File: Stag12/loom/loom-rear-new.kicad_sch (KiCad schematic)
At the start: 28 parts, among them J12 XT60H-M, J19 ASHD114-1SN-S25, J3 RING TERMINAL ON MAIN ROLL HO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

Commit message: Renamed EXC to PWR in rear loom
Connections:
- net ACCU.EXC renamed ACCU.PWR
- net BRAKE.LIGHT.EXC renamed BRAKE.LIGHT.PWR
- net BSPD.CUR_SEN.EXC renamed BSPD.CUR_SEN.PWR
- net CAN.AB.EXC renamed AIRBRIDGE.PWR
- net CAN.B.EXC renamed CAN.B.PWR
- net CAN.F.EXC renamed CAN.F.PWR
- net DASH.EXC renamed DASH.PWR
- net FAN.EXC renamed FAN.PWR
- net HVSENSE.EXC renamed HVSENSE.PWR
- net INV.EXC renamed INV.PWR
- net L120.EXC renamed L120.PWR
- net L120.SENSOR.5V.EXC renamed L120.SENSOR.5V.PWR
- net LV_BOX.EXC renamed LV_BOX.PWR
- net MOTOR.TEMP.EXC renamed MOTOR.TEMP.PWR
- net PEDALBOX.EXC renamed PEDALBOX.PWR
- net PUMP1.EXC renamed PUMP1.PWR
- net PUMP2.EXC renamed PUMP2.PWR
- net RESOLVER.EXC renamed RESOLVER.PWR
- net SPARE.EXC renamed SPARE.PWR
- net TSAC.HVS.EXC renamed TSAC.HVS.PWR
- net TSAL.DASH.EXC renamed TSAL.DASH.PWR
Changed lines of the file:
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@@
 	)
 	(bus_alias "BSPD.CUR_SEN"
-		(members "CT.SIG" "BSPD.CUR_SEN.EXC" "BSPD.CUR_SEN.GND")
+		(members "CT.SIG" "BSPD.CUR_SEN.PWR" "BSPD.CUR_SEN.GND")
 	)
 	(bus_alias "BSPD.SIM"
@@
 	)
 	(bus_alias "DASH.REAR.SIG"
-		(members "TS.DETECTED.DASH" "DASH.TS.OFF" "TSAL.DASH.EXC")
+		(members "TS.DETECTED.DASH" "DASH.TS.OFF" "TSAL.DASH.PWR")
 	)
 	(bus_alias "INV.RS232"
@@
 	)
 	(bus_alias "ONLYFANS"
-		(members "FAN.EXC" "FAN.L.PWM" "FAN.L.TACH" "FAN.R.PWM" "FAN.R.TACH" "FAN.GND")
+		(members "FAN.PWR" "FAN.L.PWM" "FAN.L.TACH" "FAN.R.PWM" "FAN.R.TACH" "FAN.GND")
 	)
 	(bus_alias "REAR_BOX"
-		(members "FAN.EXC" "FAN.GND" "FAN.L.PWM" "FAN.R.PWM" "FAN.L.TACH" "FAN.R.TACH"
-			"BRAKE.LIGHT.EXC" "BRAKE.LIGHT.GND" "CAN.B.HIGH" "CAN.B.LOW" "CAN.B.EXC"
+		(members "FAN.PWR" "FAN.GND" "FAN.L.PWM" "FAN.R.PWM" "FAN.L.TACH" "FAN.R.TACH"
+			"BRAKE.LIGHT.PWR" "BRAKE.LIGHT.GND" "CAN.B.HIGH" "CAN.B.LOW" "CAN.B.PWR"
 			"CAN.B.GND" "WHLSPD.RL.PWR" "WHLSPD.RL.SIG" "WHLSPD.RL.GND" "WHLSPD.RR.PWR"
 			"WHLSPD.RR.SIG" "WHLSPD.RR.GND" "WHLACL.RL.PWR" "WHLACL.RL.SIG" "WHLACL.RL.GND"
@@
 	)
 	(bus_alias "RESOLVER"
-		(members "RESOLVER.EXC" "RESOLVER.GND" "RESOLVER.SIN+" "RESOLVER.SIN-"
+		(members "RESOLVER.PWR" "RESOLVER.GND" "RESOLVER.SIN+" "RESOLVER.SIN-"
 			"RESOLVER.COS+" "RESOLVER.COS-"
 		)
@@
 		)
 	)
-	(label "L120.EXC"
+	(label "L120.PWR"
 		(at 417.83 48.26 180)
 		(effects
@@
 		)
 	)
-	(label "DASH.EXC"
+	(label "DASH.PWR"
 		(at 53.975 33.02 0)
 		(effects
@@
 		)
 	)
-	(label "HVSENSE.EXC"
+	(label "HVSENSE.PWR"
 		(at 714.375 349.885 0)
 		(effects
@@
 		)
 	)
-	(label "CAN.AB.PWR"
+	(label "AIRBRIDGE.PWR"
 		(at 473.71 316.23 0)
 		(effects
@@
 		)
 	)
-	(label "CAN.AB.EXC"
+	(label "AIRBRIDGE.PWR"
 		(at 486.41 28.575 180)
 		(effects
@@
 		)
 	)
-	(label "LV_BOX.EXC"
+	(label "LV_BOX.PWR"
 		(at 486.41 23.495 180)
 		(effects
@@
 		)
 	)
-	(label "PUMP1.EXC"
+	(label "PUMP1.PWR"
 		(at 486.41 99.06 180)
 		(effects
@@
 		)
 	)
-	(label "CAN.B.EXC"
+	(label "CAN.B.PWR"
 		(at 417.83 40.64 180)
 		(effects
@@
 		)
 	)
-	(label "LV_BOX.EXC"
+	(label "LV_BOX.PWR"
 		(at 417.83 33.02 180)
 		(effects
@@
 		)
 	)
-	(label "PUMP2.EXC"
+	(label "PUMP2.PWR"
 		(at 208.28 544.83 90)
 		(effects
@@
 		)
 	)
-	(label "DASH.EXC"
+	(label "DASH.PWR"
 		(at 486.41 59.055 180)
 		(effects
@@
 		)
 	)
-	(label "CAN.AB.GND"
+	(label "AIRBRIDGE.GND"
 		(at 305.435 544.195 90)
 		(effects
@@
 		)
 	)
-	(label "BSPD.CUR_SEN.EXC"
+	(label "BSPD.CUR_SEN.PWR"
 		(at 53.975 43.18 0)
 		(effects
@@
 		)
 	)
-	(label "CAN.B.EXC"
+	(label "CAN.B.PWR"
 		(at 52.07 518.16 0)
 		(effects
@@
 		)
 	)
-	(label "CAN.B.EXC"
+	(label "CAN.B.PWR"
 		(at 52.07 449.58 0)
 		(effects
@@
 		)
 	)
-	(label "TSAL.EXC"
+	(label "TSAL.PWR"
 		(at 486.41 91.44 180)
 		(effects
@@
 		)
 	)
-	(label "INV.EXC"
+	(label "INV.PWR"
 		(at 52.07 312.42 0)
 		(effects
@@
 		)
 	)
-	(label "L120.EXC"
+	(label "L120.PWR"
 		(at 486.41 56.515 180)
 		(effects
@@
 		)
 	)
-	(label "PUMP1.EXC"
+	(label "PUMP1.PWR"
 		(at 198.12 544.83 90)
 		(effects
@@
 		)
 	)
-	(label "ACCU.EXC"
+	(label "ACCU.PWR"
 		(at 486.41 53.975 180)
 		(effects
@@
 		)
 	)
-	(label "PEDALBOX.EXC"
+	(label "PEDALBOX.PWR"
 		(at 486.41 26.035 180)
 		(effects
@@
 		)
 	)
-	(label "BSPD.CUR_SEN.EXC"
+	(label "BSPD.CUR_SEN.PWR"
 		(at 714.375 354.965 0)
 		(effects
@@
 		)
 	)
-	(label "CAN.AB.EXC"
+	(label "AIRBRIDGE.PWR"
 		(at 417.83 38.1 180)
 		(effects
@@
 		)
 	)
-	(label "TSAC.HVS.EXC"
+	(label "TSAC.HVS.PWR"
 		(at 714.375 277.495 0)
 		(effects
@@
 		)
 	)
-	(label "FAN.EXC"
+	(label "FAN.PWR"
 		(at 486.41 93.98 180)
 		(effects
@@
 		)
 	)
-	(label "DASH.EXC"
+	(label "DASH.PWR"
 		(at 417.83 50.8 180)
 		(effects
@@
 		)
 	)
-	(label "INV.EXC"
+	(label "INV.PWR"
 		(at 486.41 104.14 180)
 		(effects
@@
 		)
 	)
-	(label "L120.SENSOR.5V.EXC"
+	(label "L120.SENSOR.5V.PWR"
 		(at 719.455 497.205 0)
 		(effects
@@
 		)
 	)
-	(label "PUMP2.EXC"
+	(label "PUMP2.PWR"
 		(at 486.41 101.6 180)
 		(effects
@@
 		)
 	)
-	(label "PEDALBOX.EXC"
+	(label "PEDALBOX.PWR"
 		(at 417.83 35.56 180)
 		(effects
@@
 		)
 	)
-	(label "BRAKE.LIGHT.EXC"
+	(label "BRAKE.LIGHT.PWR"
 		(at 486.41 96.52 180)
 		(effects
@@
 		)
 	)
-	(label "MOTOR.TEMP.EXC"
+	(label "MOTOR.TEMP.PWR"
 		(at 52.07 193.04 0)
 		(effects
@@
 		)
 	)
-	(label "L120.EXC"
+	(label "L120.PWR"
 		(at 714.375 487.045 0)
 		(effects
@@
 		)
 	)
-	(label "ACCU.EXC"
+	(label "ACCU.PWR"
 		(at 417.83 45.72 180)
 		(effects
@@
 		)
 	)
-	(label "RESOLVER.EXC"
+	(label "RESOLVER.PWR"
 		(at 52.07 336.55 0)
 		(effects
@@
 		)
 	)
-	(label "BRAKE.LIGHT.EXC"
+	(label "BRAKE.LIGHT.PWR"
 		(at 52.07 502.92 0)
 		(effects
@@
 		)
 	)
-	(label "TSAL.DASH.EXC"
+	(label "TSAL.DASH.PWR"
 		(at 714.375 219.075 0)
 		(effects
@@
 		)
 	)
-	(label "FAN.EXC"
+	(label "FAN.PWR"
 		(at 52.07 487.68 0)
 		(effects
@@
 		)
 	)
-	(label "CAN.F.EXC"
+	(label "CAN.F.PWR"
 		(at 486.41 51.435 180)
 		(effects
@@
 		)
 	)
-	(label "RESOLVER.EXC"
+	(label "RESOLVER.PWR"
 		(at 52.07 297.18 0)
 		(effects
@@
 		)
 	)
-	(label "L120.SENSOR.5V.EXC"
+	(label "L120.SENSOR.5V.PWR"
 		(at 714.375 423.545 0)
 		(effects
@@
 		)
 	)
-	(label "TSAL.DASH.EXC"
+	(label "TSAL.DASH.PWR"
 		(at 53.975 66.04 0)
 		(effects
@@
 		)
 	)
-	(label "CAN.F.EXC"
+	(label "CAN.F.PWR"
 		(at 417.83 43.18 180)
 		(effects
@@
 		)
 	)
-	(label "CAN.B.EXC"
+	(label "CAN.B.PWR"
 		(at 486.41 48.895 180)
 		(effects
@@
 		)
 	)
-	(label "CAN.AB.GND"
+	(label "AIRBRIDGE.GND"
 		(at 473.71 318.77 0)
 		(effects
@@
 		)
 	)
-	(label "CAN.B.EXC"
+	(label "CAN.B.PWR"
 		(at 52.07 469.265 0)
 		(effects
@@
 		)
 	)
-	(label "TSAL.EXC"
+	(label "TSAL.PWR"
 		(at 715.01 55.88 0)
 		(effects
@@
 		)
 	)
-	(label "HVSENSE.EXC"
+	(label "HVSENSE.PWR"
 		(at 714.375 259.715 0)
 		(effects
@@
 		)
 	)
-	(label "PEDALBOX.EXC"
+	(label "PEDALBOX.PWR"
 		(at 53.975 55.88 0)
 		(effects
@@
 		)
 	)
-	(label "SPARE.EXC"
+	(label "SPARE.PWR"
 		(at 719.455 522.605 0)
 		(effects
@@
 		)
 	)
-	(label "LV_BOX.EXC"
+	(label "LV_BOX.PWR"
 		(at 714.375 213.995 0)
 		(effects
@@
 		)
 	)
-	(label "ACCU.EXC"
+	(label "ACCU.PWR"
 		(at 715.01 60.96 0)
 		(effects

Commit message: Reserved Autosport for pedalbox
Pedal box loom near completion, pending connector spec

VCU is now connector hell
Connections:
- net PEDALBOX.PWR: no longer Conn20.13
- net BSPD.PWR: now reaches Conn30.9
- net BSPD.PWR: now also Conn20.13
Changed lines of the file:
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@@
 	)
 	(bus_entry
-		(at 462.915 157.48)
+		(at 454.025 157.48)
 		(size 2.54 -2.54)
 		(stroke
@@
 	)
 	(bus_entry
-		(at 462.915 152.4)
+		(at 454.025 152.4)
 		(size 2.54 -2.54)
 		(stroke
@@
 	)
 	(bus_entry
-		(at 462.915 160.02)
+		(at 454.025 160.02)
 		(size 2.54 -2.54)
 		(stroke
@@
 	)
 	(bus_entry
-		(at 462.915 154.94)
+		(at 454.025 154.94)
 		(size 2.54 -2.54)
 		(stroke
@@
 		)
 	)
+	(wire
+		(pts
+			(xy 495.3 160.02) (xy 460.375 160.02)
+		)
+		(stroke
+			(width 0)
+			(type default)
+		)
+	)
 	(polyline
 		(pts
@@
 	(wire
 		(pts
-			(xy 465.455 149.86) (xy 495.3 149.86)
+			(xy 456.565 149.86) (xy 495.3 149.86)
 		)
 		(stroke
@@
 		)
 	)
-	(wire
-		(pts
-			(xy 417.83 35.56) (xy 365.125 35.56)
-		)
-		(stroke
-			(width 0)
-			(type default)
-		)
-	)
 	(polyline
 		(pts
@@
 	(wire
 		(pts
+			(xy 460.375 160.02) (xy 460.375 162.56)
+		)
+		(stroke
+			(width 0)
+			(type default)
+		)
+	)
+	(wire
+		(pts
 			(xy 441.325 295.91) (xy 441.325 236.855)
 		)
@@
 	(bus
 		(pts
-			(xy 462.915 186.055) (xy 467.995 191.135)
+			(xy 454.025 186.055) (xy 459.105 191.135)
 		)
 		(stroke
@@
 	(bus
 		(pts
-			(xy 467.995 191.135) (xy 648.97 191.135)
+			(xy 459.105 191.135) (xy 648.97 191.135)
 		)
 		(stroke
@@
 	(bus
 		(pts
-			(xy 462.915 154.94) (xy 462.915 157.48)
+			(xy 454.025 154.94) (xy 454.025 157.48)
 		)
 		(stroke
@@
 		)
 	)
+	(wire
+		(pts
+			(xy 382.905 162.56) (xy 460.375 162.56)
+		)
+		(stroke
+			(width 0)
+			(type default)
+		)
+	)
 	(bus
 		(pts
@@
 	(wire
 		(pts
-			(xy 465.455 157.48) (xy 495.3 157.48)
+			(xy 456.565 157.48) (xy 495.3 157.48)
 		)
 		(stroke
@@
 	(wire
 		(pts
-			(xy 465.455 154.94) (xy 495.3 154.94)
+			(xy 456.565 154.94) (xy 495.3 154.94)
 		)
 		(stroke
@@
 	(wire
 		(pts
-			(xy 365.125 35.56) (xy 365.125 55.88)
-		)
-		(stroke
-			(width 0)
-			(type default)
-		)
-	)
-	(wire
-		(pts
 			(xy 748.03 226.695) (xy 694.69 226.695)
 		)
@@
 	(bus
 		(pts
-			(xy 462.915 160.02) (xy 462.915 186.055)
+			(xy 454.025 160.02) (xy 454.025 186.055)
 		)
 		(stroke
@@
 	(wire
 		(pts
-			(xy 465.455 152.4) (xy 495.3 152.4)
+			(xy 456.565 152.4) (xy 495.3 152.4)
 		)
 		(stroke
@@
 	(bus
 		(pts
-			(xy 462.915 157.48) (xy 462.915 160.02)
+			(xy 454.025 157.48) (xy 454.025 160.02)
 		)
 		(stroke
@@
 	(wire
 		(pts
-			(xy 52.07 55.88) (xy 365.125 55.88)
+			(xy 52.07 55.88) (xy 382.905 55.88)
 		)
 		(stroke
@@
 	(bus
 		(pts
-			(xy 462.915 152.4) (xy 462.915 154.94)
+			(xy 454.025 152.4) (xy 454.025 154.94)
 		)
 		(stroke
@@
 	(wire
 		(pts
+			(xy 381 35.56) (xy 417.83 35.56)
+		)
+		(stroke
+			(width 0)
+			(type default)
+		)
+	)
+	(wire
+		(pts
 			(xy 74.93 409.575) (xy 74.93 422.275)
 		)
@@
 	(wire
 		(pts
+			(xy 382.905 55.88) (xy 382.905 162.56)
+		)
+		(stroke
+			(width 0)
+			(type default)
+		)
+	)
+	(wire
+		(pts
 			(xy 210.82 513.08) (xy 210.82 544.83)
 		)
@@
 		)
 	)
-	(label "PEDALBOX.PWR"
+	(label "BSPD.PWR"
 		(at 53.975 55.88 0)
 		(effects
@@
 		(effects
 			(font
+				(size 1.27 1.27)
+			)
+			(justify left bottom)
+		)
+	)
+	(label "BSPD.PWR"
+		(at 476.885 160.02 0)
+		(effects
+			(font

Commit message: More progress on front loom
autosport my beloved
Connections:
- net BSPD.CUR_SEN.SIG is gone; now on net CT.SIG: Conn74.6
- net CAN.F.PWR: now also Conn20.26
- net CAN.C.L: now reaches Conn20.46
- net CAN.C.L: now also Conn17.18, Conn22.11, Conn31.9, Conn50.20, Conn50.36, Conn51.1, Conn53.1
- net CAN.C.H: now reaches Conn20.47
- net CAN.C.H: now also Conn17.19, Conn22.33, Conn31.10, Conn50.19, Conn50.35, Conn51.2, Conn53.2
- net BSPD.CUR_SEN.GND: no longer names the net of Conn20.9
- net BSPD.CUR_SEN.GND: no longer Conn74.5
- net BSPD.CUR_SEN.PWR renamed BSPD.CT.PWR
- net BSPD.CT.PWR: now also Conn20.2; no longer Conn20.8
- removed net CAN.C.HIGH: Conn17.19, Conn20.3, Conn22.33, Conn31.10, Conn50.19, Conn50.35, Conn51.2, Conn53.2
- removed net CAN.C.LOW: Conn17.18, Conn20.2, Conn22.11, Conn31.9, Conn50.20, Conn50.36, Conn51.1, Conn53.1
- new net BSPD.CT.GND: Conn20.3, Conn74.5
- new net BSPD.CT.SHLD: Conn20.8
- no-connect marks 46 -> 44

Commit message: Rear loom nearly complete
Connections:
- net CAN.F.PWR: now also Conn20.43; no longer Conn20.26
- net L120.AV1: now reaches Conn20.27
- net L120.AV2: now reaches Conn20.28
- net L120.AV3: now reaches Conn20.29
- net L120.AV4: now reaches Conn20.30
- net L120.AV5: now reaches Conn20.31
- net L120.AV6: now reaches Conn20.32
- net CAN.F.GND: now reaches Conn20.42
- net CAN.F.H: now reaches Conn20.44
- net CAN.F.H: now also Conn50.27
- net CAN.F.L: now reaches Conn20.45
- net CAN.F.L: now also Conn50.28
- net CAN.F.HIGH renamed L120.5V.AUX
- net L120.5V.AUX: no longer Conn50.27
- net CAN.F.LOW renamed L120.8V.AUX
- net L120.8V.AUX: no longer Conn50.28
- net PEDALBOX.PWR: no longer names the net of Conn31.2, Conn51.4
- net PEDALBOX.PWR: no longer Conn53.4
- new net L120.AGND.SHLD: Conn20.26
- no-connect marks 44 -> 43
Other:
- moved on the sheet: Conn30, Conn31, Conn32, J19

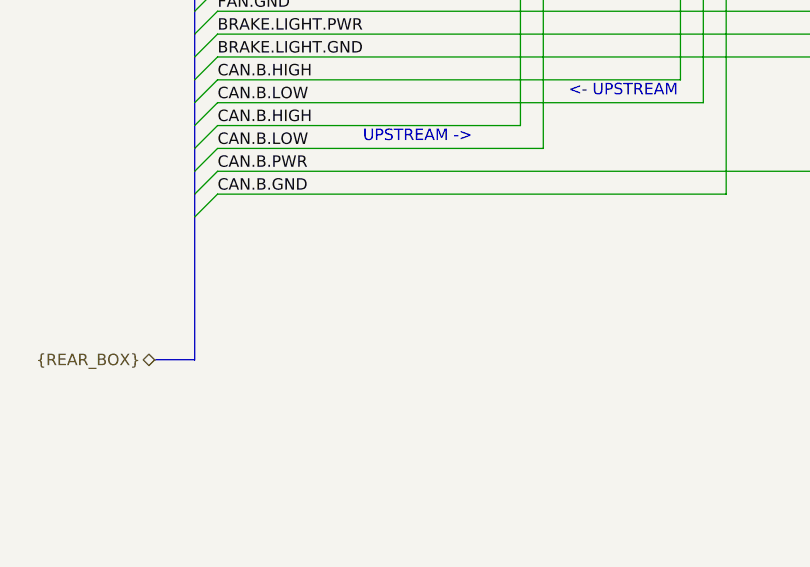
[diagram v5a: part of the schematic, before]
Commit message: More loom notes
autosport crimp selection hell
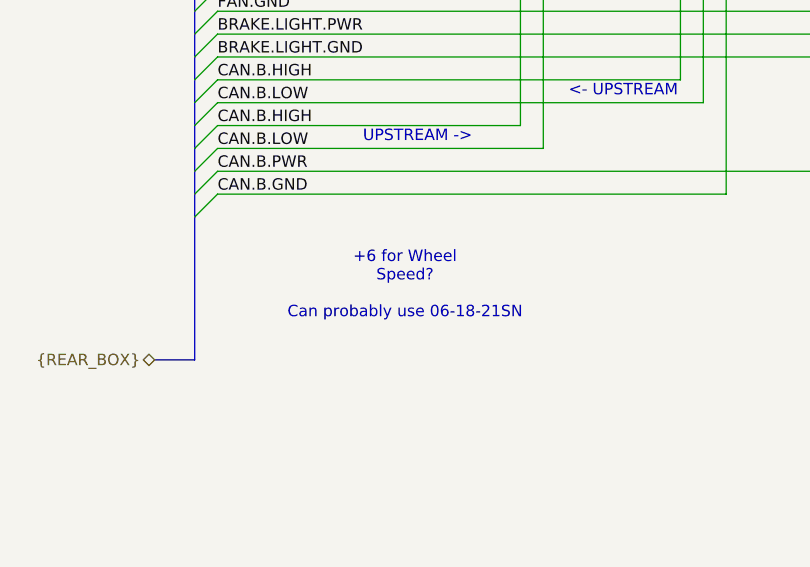
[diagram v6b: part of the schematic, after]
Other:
- note added: "+6 for Wheel Speed? Can probably use 06-18-21SN"
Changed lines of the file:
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@@
+		)
+	)
+	(text "+6 for Wheel\nSpeed?\n\nCan probably use 06-18-21SN"
+		(exclude_from_sim no)
+		(at 72.898 530.86 0)
+		(effects
+			(font
+				(size 1.27 1.27)
+			)
 		)
 	)

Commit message: idfk
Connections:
- net L120.AGND.SHLD is gone; now on net CAN.F.PWR: Conn20.26
- net CAN.F.PWR: no longer Conn20.43
- net PEDALBOX.PWR: now reaches Conn31.2, Conn51.4
- net PEDALBOX.PWR: now also Conn53.4
- net CAN.F.GND: no longer names the net of Conn20.42
- net CAN.F.H: no longer names the net of Conn20.44
- net CAN.F.H: no longer Conn50.27
- net CAN.F.L: no longer names the net of Conn20.45
- net CAN.F.L: no longer Conn50.28
- net L120.5V.AUX renamed CAN.F.HIGH
- net CAN.F.HIGH: now also Conn50.27
- net L120.8V.AUX renamed CAN.F.LOW
- net CAN.F.LOW: now also Conn50.28
- net L120.AV1: no longer names the net of Conn20.27
- net L120.AV2: no longer names the net of Conn20.28
- net L120.AV3: no longer names the net of Conn20.29
- net L120.AV4: no longer names the net of Conn20.30
- net L120.AV5: no longer names the net of Conn20.31
- net L120.AV6: no longer names the net of Conn20.32
- no-connect marks 43 -> 44
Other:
- note added: "/\ ???"
- note added: "???"
- note removed: "+6 for Wheel Speed? Can probably use 06-18-21SN"
- moved on the sheet: Conn30, Conn31, Conn32, J19

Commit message: Updated connector locations
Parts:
- removed Conn72: TODO: CHECK CONNECTOR, symbol Connectors_SUFST:Current Sensor Connector
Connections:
- net INV.PWR: now also Conn23.8
- net RESOLVER.PWR: no longer Conn23.17
- net IN.4: now reaches Conn31.16
- net IN.5: now reaches Conn31.17
- net IN.6: now reaches Conn31.18
- net IN.7: now reaches Conn31.19
- net IN.8: now reaches Conn31.20
- net IN.9: now reaches Conn31.21
- net IN.10: now reaches Conn31.22
- net IN.11: now reaches Conn31.23
- net IN.12: now reaches Conn31.24
- net IN.1: now reaches Conn31.4
- net IN.2: now reaches Conn31.5
- net IN.3: now reaches Conn31.6
- net PDM.GNDREF: now reaches Conn31.7
- net PDM.GNDREF: now also Conn31.8
- new net RESOLVER.EXC: Conn23.17
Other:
- note added: "FSG RJ45 on bonus hole"
- note added: "TODO: Change to autosport?"
- note removed: "TODO: CHECK USB CONNECTOR"
- note removed: "USB"
